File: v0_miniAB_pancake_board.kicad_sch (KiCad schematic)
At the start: 13 parts, among them J1 E_STEPPER, J10 FAN0_V_JUMPER, J11 FAN1_V_JUMPER, J12 RGB LED, J13 BLTOUCH, J2 HEATER, J3 THERM, J4 PART FAN, J5 PART FAN, J6 HOTEND FAN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

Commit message: Added traces, pushing for review.
Please review
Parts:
- added H1, H2: MountingHole_Pad, MountingHole:MountingHole_3.2mm_M3_Pad, symbol Mechanical:MountingHole_Pad
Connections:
- net +24V: now also J2.2 (Pin_2); no longer J2.1 (Pin_1)
- net GND: now also H1.1, H2.1
- net heat_gnd: now also J2.1 (Pin_1); no longer J2.2 (Pin_2)
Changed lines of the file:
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@@
   (junction (at 49.53 55.88) (diameter 0) (color 0 0 0 0)
   )
+  (junction (at 119.38 160.02) (diameter 0) (color 0 0 0 0)
+  )
+  (wire (pts (xy 119.38 160.02) (xy 119.38 168.91))
+    (stroke (width 0) (type default) (color 0 0 0 0))
+  )
   (wire (pts (xy 49.53 55.88) (xy 57.15 55.88))
     (stroke (width 0) (type default) (color 0 0 0 0))
@@
     (stroke (width 0) (type default) (color 0 0 0 0))
   )
+  (wire (pts (xy 119.38 152.4) (xy 119.38 160.02))
+    (stroke (width 0) (type default) (color 0 0 0 0))
+  )
   (wire (pts (xy 116.84 36.83) (xy 128.27 36.83))
     (stroke (width 0) (type default) (color 0 0 0 0))
@@
     (stroke (width 0) (type default) (color 0 0 0 0))
   )
+  (wire (pts (xy 46.99 26.67) (xy 45.72 26.67))
+    (stroke (width 0) (type default) (color 0 0 0 0))
+  )
   (wire (pts (xy 45.72 55.88) (xy 49.53 55.88))
     (stroke (width 0) (type default) (color 0 0 0 0))
   )
-  (wire (pts (xy 45.72 26.67) (xy 57.15 26.67))
-    (stroke (width 0) (type default) (color 0 0 0 0))
-  )
   (wire (pts (xy 45.72 78.74) (xy 57.15 78.74))
     (stroke (width 0) (type default) (color 0 0 0 0))
@@
     (stroke (width 0) (type default) (color 0 0 0 0))
   )
+  (wire (pts (xy 140.97 34.29) (xy 152.4 34.29))
+    (stroke (width 0) (type default) (color 0 0 0 0))
+  )
+  (wire (pts (xy 49.53 55.88) (xy 49.53 67.31))
+    (stroke (width 0) (type default) (color 0 0 0 0))
+  )
+  (wire (pts (xy 128.27 26.67) (xy 116.84 26.67))
+    (stroke (width 0) (type default) (color 0 0 0 0))
+  )
   (wire (pts (xy 45.72 29.21) (xy 57.15 29.21))
     (stroke (width 0) (type default) (color 0 0 0 0))
   )
-  (wire (pts (xy 140.97 34.29) (xy 152.4 34.29))
-    (stroke (width 0) (type default) (color 0 0 0 0))
-  )
-  (wire (pts (xy 49.53 55.88) (xy 49.53 67.31))
-    (stroke (width 0) (type default) (color 0 0 0 0))
-  )
-  (wire (pts (xy 128.27 26.67) (xy 116.84 26.67))
+  (wire (pts (xy 119.38 160.02) (xy 125.73 160.02))
     (stroke (width 0) (type default) (color 0 0 0 0))
   )
@@
     (stroke (width 0) (type default) (color 0 0 0 0))
   )
+  (wire (pts (xy 125.73 152.4) (xy 119.38 152.4))
+    (stroke (width 0) (type default) (color 0 0 0 0))
+  )
   (wire (pts (xy 76.2 53.34) (xy 87.63 53.34))
     (stroke (width 0) (type default) (color 0 0 0 0))
@@
     (effects (font (size 1.27 1.27)) (justify left bottom))
   )
-  (label "heat_gnd" (at 48.26 29.21 0)
+  (label "heat_gnd" (at 46.99 26.67 0)
     (effects (font (size 1.27 1.27)) (justify left bottom))
   )
@@
     (pin "1")
   )
-  (symbol (lib_id "power:+24V") (at 57.15 26.67 0) (unit 1)
-    (in_bom yes) (on_board yes)
-    (property "Reference" "#PWR0105" (id 0) (at 57.15 30.48 0)
-      (effects (font (size 1.27 1.27)) hide)
-    )
-    (property "Value" "+24V" (id 1) (at 57.15 24.13 90)
-      (effects (font (size 1.27 1.27)) (justify left))
-    )
-    (property "Footprint" "" (id 2) (at 57.15 26.67 0)
-      (effects (font (size 1.27 1.27)) hide)
-    )
-    (property "Datasheet" "" (id 3) (at 57.15 26.67 0)
-      (effects (font (size 1.27 1.27)) hide)
-    )
-    (pin "1")
-  )
   (symbol (lib_id "Connector:Conn_01x03_Female") (at 81.28 81.28 0) (mirror y) (unit 1)
     (in_bom yes) (on_board yes)
@@
     (pin "1")
   )
+  (symbol (lib_id "power:GND") (at 119.38 168.91 0) (unit 1)
+    (in_bom yes) (on_board yes)
+    (property "Reference" "#PWR012" (id 0) (at 119.38 175.26 0)
+      (effects (font (size 1.27 1.27)) hide)
+    )
+    (property "Value" "GND" (id 1) (at 119.507 172.1612 90)
+      (effects (font (size 1.27 1.27)) (justify right))
+    )
+    (property "Footprint" "" (id 2) (at 119.38 168.91 0)
+      (effects (font (size 1.27 1.27)) hide)
+    )
+    (property "Datasheet" "" (id 3) (at 119.38 168.91 0)
+      (effects (font (size 1.27 1.27)) hide)
+    )
+    (pin "1")
+  )
   (symbol (lib_id "power:GND") (at 151.13 74.93 90) (unit 1)
     (in_bom yes) (on_board yes)
@@
     )
     (property "Datasheet" "" (id 3) (at 151.13 74.93 0)
+      (effects (font (size 1.27 1.27)) hide)
+    )
+    (pin "1")
+  )
+  (symbol (lib_id "Mechanical:MountingHole_Pad") (at 125.73 149.86 0) (unit 1)
+    (in_bom yes) (on_board yes) (fields_autoplaced)
+    (property "Reference" "H1" (id 0) (at 128.27 147.6815 0)
+      (effects (font (size 1.27 1.27)) (justify left))
+    )
+    (property "Value" "MountingHole_Pad" (id 1) (at 128.27 150.4566 0)
+      (effects (font (size 1.27 1.27)) (justify left))
+    )
+    (property "Footprint" "MountingHole:MountingHole_3.2mm_M3_Pad" (id 2) (at 125.73 149.86 0)
+      (effects (font (size 1.27 1.27)) hide)
+    )
+    (property "Datasheet" "~" (id 3) (at 125.73 149.86 0)
+      (effects (font (size 1.27 1.27)) hide)
+    )
+    (pin "1")
+  )
+  (symbol (lib_id "power:+24V") (at 57.15 29.21 0) (unit 1)
+    (in_bom yes) (on_board yes)
+    (property "Reference" "#PWR?" (id 0) (at 57.15 33.02 0)
+      (effects (font (size 1.27 1.27)) hide)
+    )
+    (property "Value" "+24V" (id 1) (at 57.15 26.67 90)
+      (effects (font (size 1.27 1.27)) (justify left))
+    )
+    (property "Footprint" "" (id 2) (at 57.15 29.21 0)
+      (effects (font (size 1.27 1.27)) hide)
+    )
+    (property "Datasheet" "" (id 3) (at 57.15 29.21 0)
       (effects (font (size 1.27 1.27)) hide)
     )
@@
     )
     (property "Datasheet" "" (id 3) (at 100.33 118.11 0)
+      (effects (font (size 1.27 1.27)) hide)
+    )
+    (pin "1")
+  )
+  (symbol (lib_id "Mechanical:MountingHole_Pad") (at 125.73 157.48 0) (unit 1)
+    (in_bom yes) (on_board yes) (fields_autoplaced)
+    (property "Reference" "H2" (id 0) (at 128.27 155.3015 0)
+      (effects (font (size 1.27 1.27)) (justify left))
+    )
+    (property "Value" "MountingHole_Pad" (id 1) (at 128.27 158.0766 0)
+      (effects (font (size 1.27 1.27)) (justify left))
+    )
+    (property "Footprint" "MountingHole:MountingHole_3.2mm_M3_Pad" (id 2) (at 125.73 157.48 0)
+      (effects (font (size 1.27 1.27)) hide)
+    )
+    (property "Datasheet" "~" (id 3) (at 125.73 157.48 0)
       (effects (font (size 1.27 1.27)) hide)
     )
@@
       (reference "#PWR011") (unit 1) (value "GND") (footprint "")
     )
+    (path "/011fdab8-ed4c-4a2a-a007-da8c57df54f0"
+      (reference "#PWR012") (unit 1) (value "GND") (footprint "")
+    )
     (path "/00000000-0000-0000-0000-0000612c2dd0"
       (reference "#PWR0101") (unit 1) (value "+5V") (footprint "")
@@
       (reference "#PWR0104") (unit 1) (value "+24V") (footprint "")
     )
-    (path "/00000000-0000-0000-0000-0000612bf736"
-      (reference "#PWR0105") (unit 1) (value "+24V") (footprint "")
-    )
     (path "/00000000-0000-0000-0000-0000612b9e54"
       (reference "#PWR0106") (unit 1) (value "+24V") (footprint "")
     )
+    (path "/963cdc5d-c7c3-42c2-8cac-83120971b91e"
+      (reference "#PWR?") (unit 1) (value "+24V") (footprint "")
+    )
+    (path "/1c4ead20-ff6c-4333-ae02-f15822b6e8ec"
+      (reference "H1") (unit 1) (value "MountingHole_Pad") (footprint "MountingHole:MountingHole_3.2mm_M3_Pad")
+    )
+    (path "/bc956c90-beba-4015-ae6e-0995800a545f"
+      (reference "H2") (unit 1) (value "MountingHole_Pad") (footprint "MountingHole:MountingHole_3.2mm_M3_Pad")
+    )
     (path "/00000000-0000-0000-0000-000060d55abc"

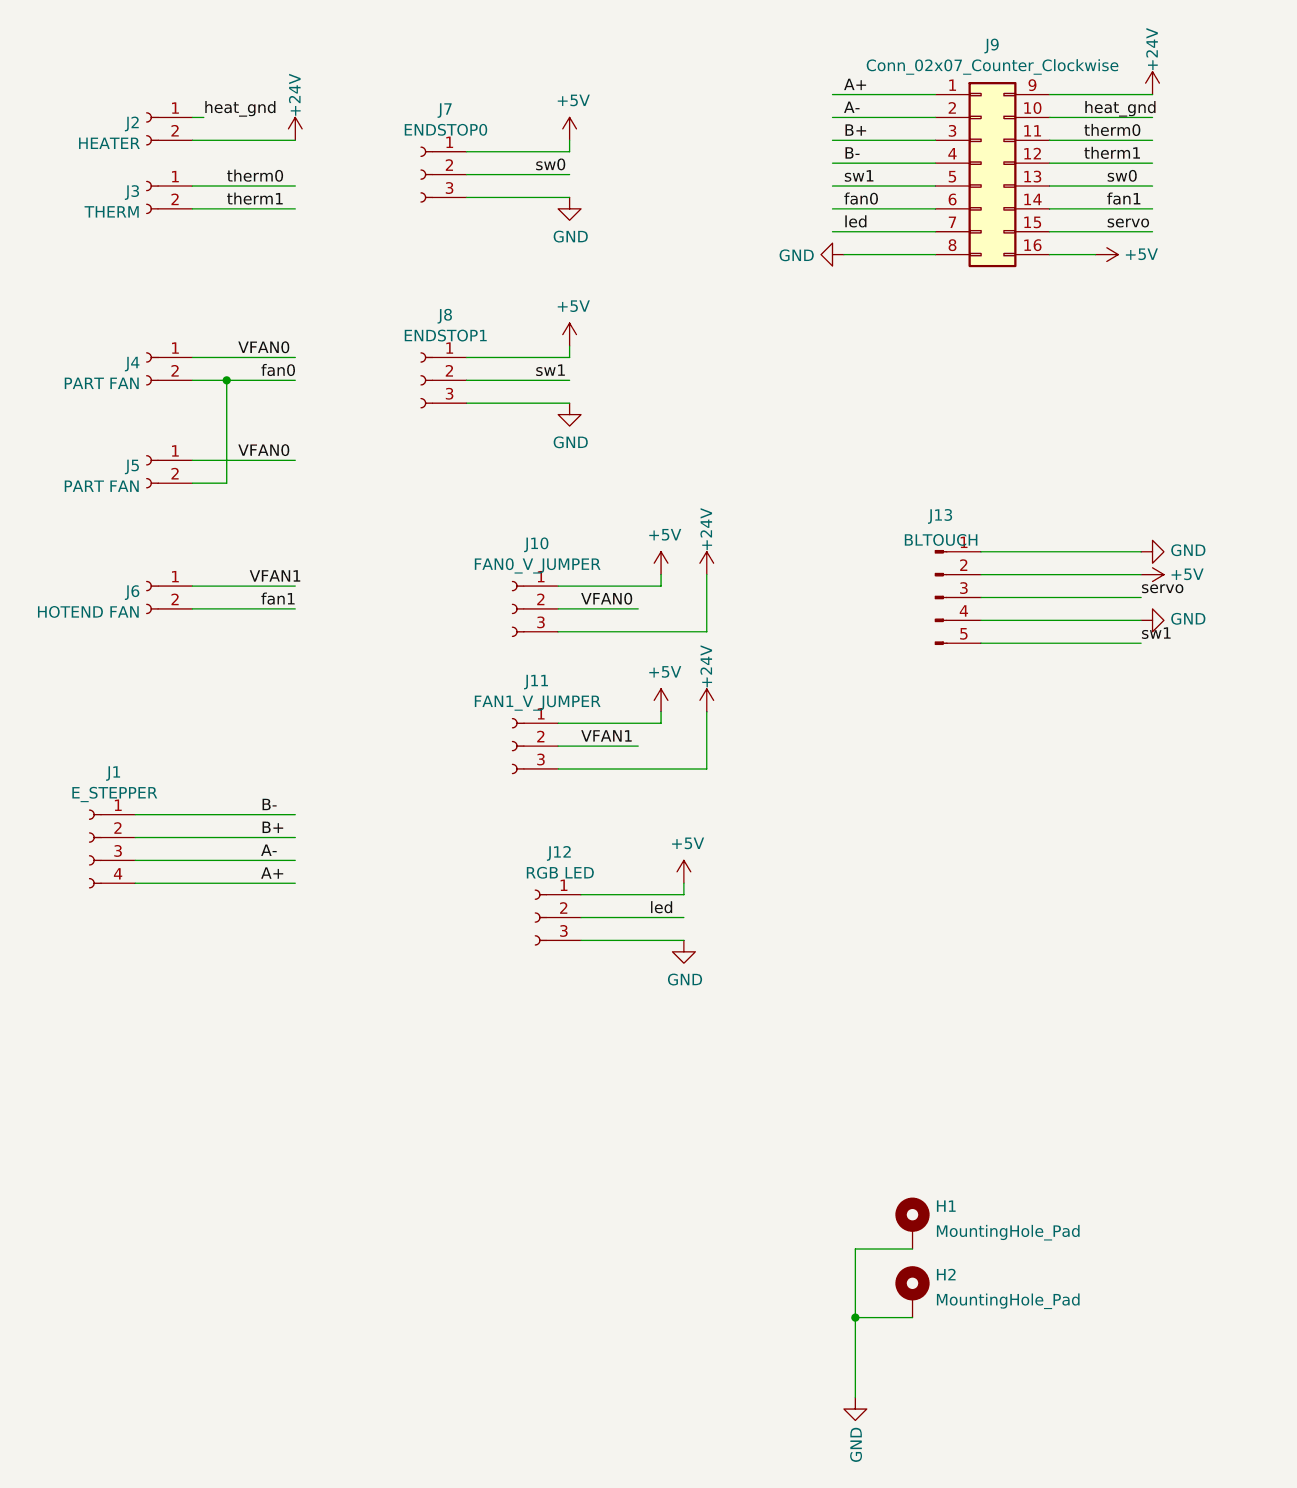
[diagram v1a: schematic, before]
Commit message: Adjusted after comments
Fixed some pin orientations and pin assignments in the schematic.
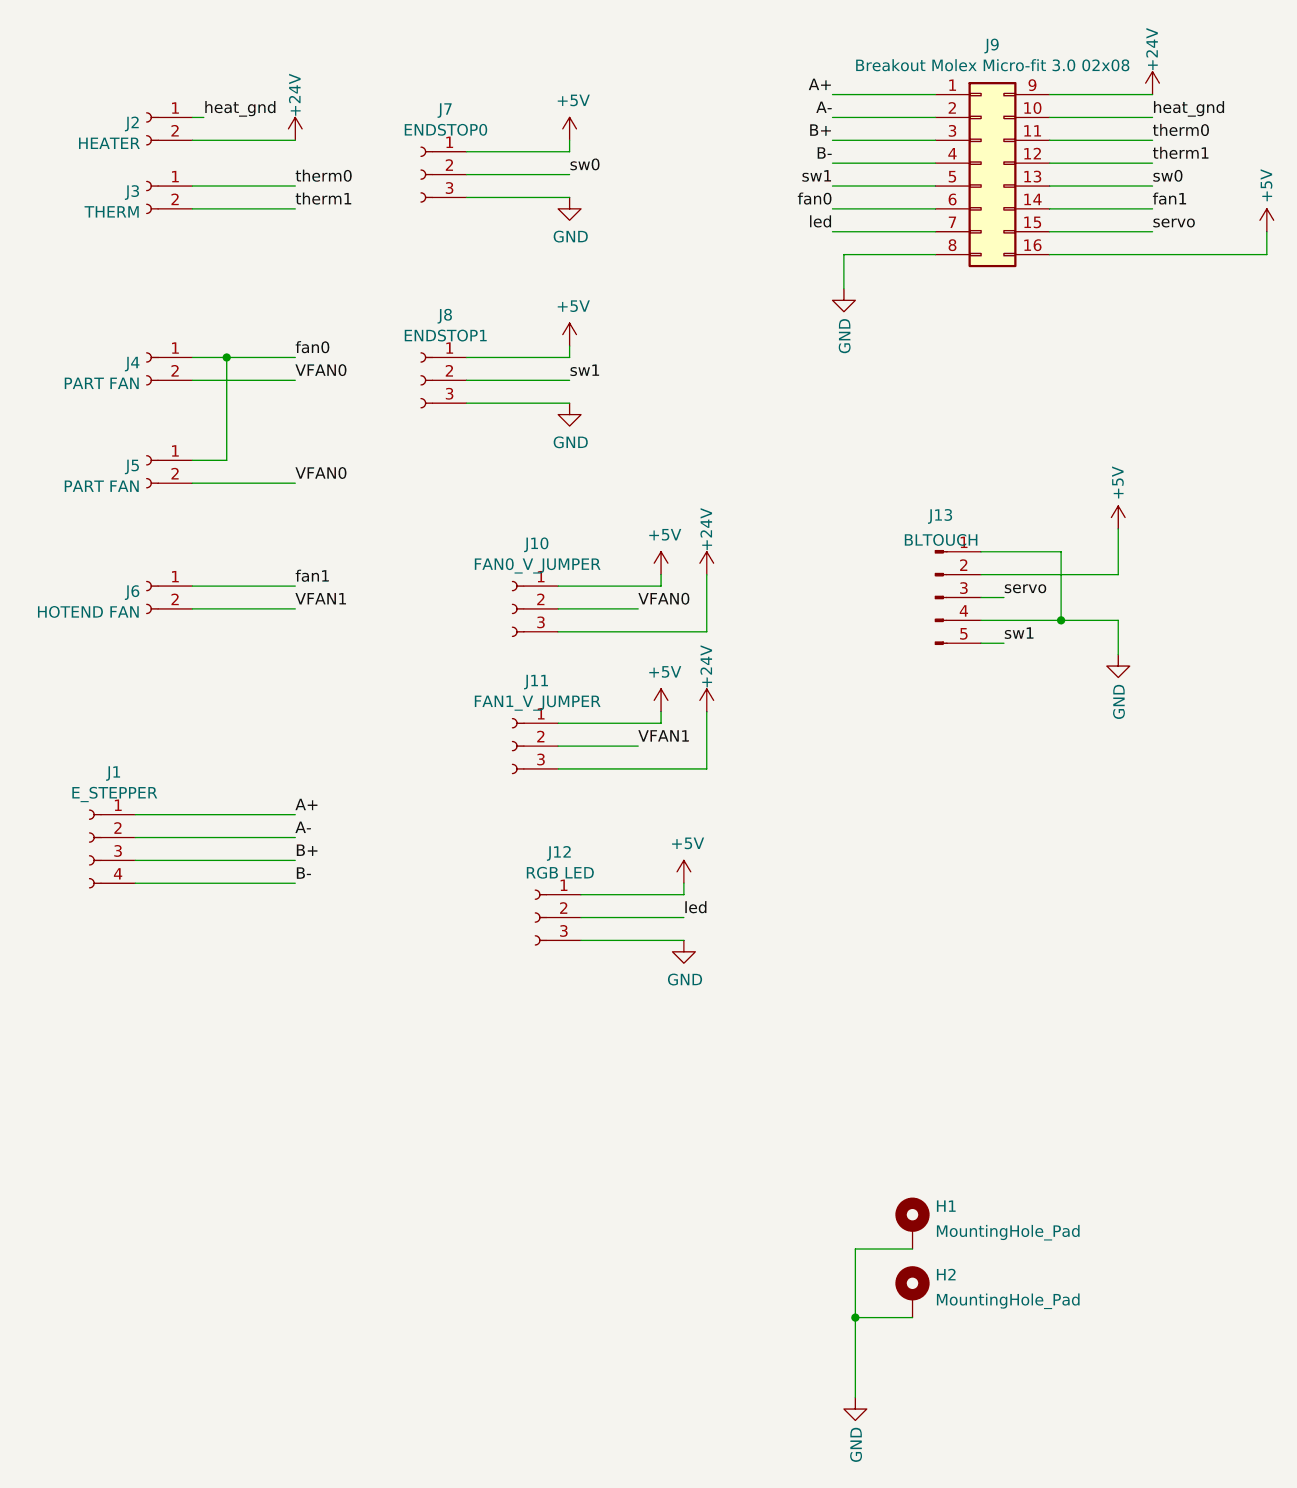
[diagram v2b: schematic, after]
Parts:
- J9: value Conn_02x07_Counter_Clockwise -> Breakout Molex Micro-fit 3.0 02x08
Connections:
- net A+: now also J1.1 (Pin_1); no longer J1.4 (Pin_4)
- net A-: now also J1.2 (Pin_2); no longer J1.3 (Pin_3)
- net B+: now also J1.3 (Pin_3); no longer J1.2 (Pin_2)
- net B-: now also J1.4 (Pin_4); no longer J1.1 (Pin_1)
- net VFAN0: now also J4.2 (Pin_2), J5.2 (Pin_2); no longer J4.1 (Pin_1), J5.1 (Pin_1)
- net VFAN1: now also J6.2 (Pin_2); no longer J6.1 (Pin_1)
- net fan0: now also J4.1 (Pin_1), J5.1 (Pin_1); no longer J4.2 (Pin_2), J5.2 (Pin_2)
- net fan1: now also J6.1 (Pin_1); no longer J6.2 (Pin_2)

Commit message: Fix connectors direction and organize routes
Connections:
- net A+: now also J1.4 (Pin_4); no longer J1.1 (Pin_1)
- net A-: now also J1.3 (Pin_3); no longer J1.2 (Pin_2)
- net B+: now also J1.2 (Pin_2); no longer J1.3 (Pin_3)
- net B-: now also J1.1 (Pin_1); no longer J1.4 (Pin_4)
- net VFAN0: now also J4.1 (Pin_1), J5.1 (Pin_1); no longer J4.2 (Pin_2), J5.2 (Pin_2)
- net VFAN1: now also J6.1 (Pin_1); no longer J6.2 (Pin_2)
- net fan0: now also J4.2 (Pin_2), J5.2 (Pin_2); no longer J4.1 (Pin_1), J5.1 (Pin_1)
- net fan1: now also J6.2 (Pin_2); no longer J6.1 (Pin_1)
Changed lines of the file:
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@@
     (stroke (width 0) (type default) (color 0 0 0 0))
   )
-  (label "A-" (at 57.15 106.68 0)
+  (label "A+" (at 57.15 111.76 0)
     (effects (font (size 1.27 1.27)) (justify left bottom))
   )
@@
     (effects (font (size 1.27 1.27)) (justify left bottom))
   )
-  (label "B-" (at 57.15 111.76 0)
+  (label "therm0" (at 57.15 34.29 0)
     (effects (font (size 1.27 1.27)) (justify left bottom))
   )
-  (label "therm0" (at 57.15 34.29 0)
+  (label "B-" (at 57.15 104.14 0)
     (effects (font (size 1.27 1.27)) (justify left bottom))
   )
@@
     (effects (font (size 1.27 1.27)) (justify right bottom))
   )
-  (label "VFAN0" (at 57.15 67.31 0)
-    (effects (font (size 1.27 1.27)) (justify left bottom))
-  )
   (label "sw1" (at 135.89 85.09 0)
     (effects (font (size 1.27 1.27)) (justify left bottom))
   )
   (label "therm0" (at 152.4 29.21 0)
+    (effects (font (size 1.27 1.27)) (justify left bottom))
+  )
+  (label "VFAN1" (at 57.15 78.74 0)
+    (effects (font (size 1.27 1.27)) (justify left bottom))
+  )
+  (label "fan1" (at 57.15 81.28 0)
+    (effects (font (size 1.27 1.27)) (justify left bottom))
+  )
+  (label "B+" (at 57.15 106.68 0)
+    (effects (font (size 1.27 1.27)) (justify left bottom))
+  )
+  (label "A-" (at 57.15 109.22 0)
     (effects (font (size 1.27 1.27)) (justify left bottom))
   )
@@
     (effects (font (size 1.27 1.27)) (justify left bottom))
   )
+  (label "fan0" (at 57.15 55.88 0)
+    (effects (font (size 1.27 1.27)) (justify left bottom))
+  )
   (label "sw0" (at 87.63 33.02 0)
     (effects (font (size 1.27 1.27)) (justify left bottom))
@@
     (effects (font (size 1.27 1.27)) (justify right bottom))
   )
-  (label "fan1" (at 57.15 78.74 0)
+  (label "fan0" (at 57.15 67.31 0)
     (effects (font (size 1.27 1.27)) (justify left bottom))
   )
-  (label "fan0" (at 57.15 53.34 0)
-    (effects (font (size 1.27 1.27)) (justify left bottom))
-  )
-  (label "B+" (at 57.15 109.22 0)
+  (label "VFAN0" (at 57.15 53.34 0)
     (effects (font (size 1.27 1.27)) (justify left bottom))
   )
@@
     (effects (font (size 1.27 1.27)) (justify right bottom))
   )
-  (label "VFAN1" (at 57.15 81.28 0)
-    (effects (font (size 1.27 1.27)) (justify left bottom))
-  )
   (label "sw1" (at 87.63 55.88 0)
-    (effects (font (size 1.27 1.27)) (justify left bottom))
-  )
-  (label "A+" (at 57.15 104.14 0)
     (effects (font (size 1.27 1.27)) (justify left bottom))
   )
@@
     (effects (font (size 1.27 1.27)) (justify left bottom))
   )
-  (label "VFAN0" (at 57.15 55.88 0)
-    (effects (font (size 1.27 1.27)) (justify left bottom))
-  )
